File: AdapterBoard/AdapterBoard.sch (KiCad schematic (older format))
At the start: 80 parts, among them J1 Conn_01x06, J10 Conn_01x01, J11 Conn_01x02, J12 Conn_01x01, J13 Conn_01x02, J14 Conn_01x01, J15 Conn_01x02, J16 Conn_01x01, J17 Conn_01x02, J18 Conn_01x01, J19 Conn_01x02, J2 Conn_01x06, J20 Conn_01x01, J21 Conn_01x02, J22 Conn_01x01, J23 Conn_01x02, J24 Conn_01x01, J25 Conn_01x01, J26 Conn_01x06, J27 Conn_01x01, J28 Conn_01x04, J29 Conn_01x06, J3 Conn_01x06, J30 Conn_01x06, J31 Conn_01x04, J32 Conn_01x01, J33 Conn_01x06, J34 Conn_01x01, J35 Conn_01x01, J36 Conn_01x01, J37 Conn_01x01, J38 Conn_01x06, J39 Conn_01x01, J4 Conn_01x06, J40 Conn_01x04, J41 Conn_01x06, J42 Conn_01x06, J43 Conn_01x04, J44 Conn_01x01, J45 Conn_01x06, J46 Conn_01x01, J47 Conn_01x01, J48 Conn_01x06, J49 Conn_01x04, J5 Conn_01x06, J50 Conn_01x01, J51 Conn_01x06, J52 Conn_01x01, J53 Conn_01x01, J54 Conn_01x06, J55 Conn_01x04, J56 Conn_01x01, J57 Conn_01x06, J58 Conn_01x01, J59 Conn_01x04, J6 Conn_01x06, J60 Conn_02x13_Odd_Even, J61 Conn_01x04, J62 Conn_01x04, J63 Conn_01x13, J64 Conn_01x13, J7 Conn_01x06, J8 Conn_01x06, J9 Conn_01x02

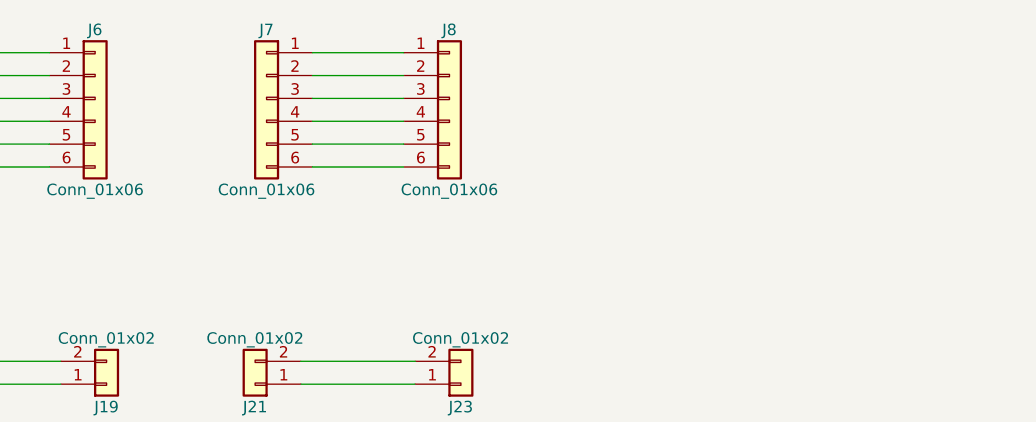
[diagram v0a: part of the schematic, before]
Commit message: Added CAD models
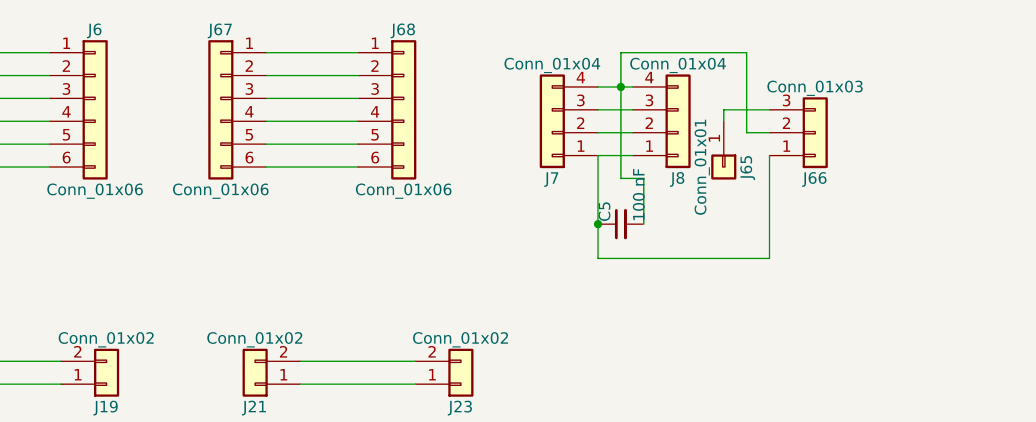
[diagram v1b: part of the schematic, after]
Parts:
- removed J7, J8: Conn_01x06, Pin_Headers:Pin_Header_Straight_1x06_Pitch2.54mm, symbol Conn_01x06
- added C5: 100 nF, Capacitors_THT:C_Disc_D5.0mm_W2.5mm_P2.50mm, symbol C_Small
- added J65: Conn_01x01, Pin_Headers:Pin_Header_Straight_1x01_Pitch2.54mm, symbol Conn_01x01
- added J66: Conn_01x03, TO_SOT_Packages_THT:TO-92_Inline_Wide, symbol Conn_01x03
- added J67, J68: Conn_01x06, Pin_Headers:Pin_Header_Straight_1x06_Pitch2.54mm, symbol Conn_01x06
- added J7, J8: Conn_01x04, Pin_Headers:Pin_Header_Straight_1x04_Pitch2.54mm, symbol Conn_01x04
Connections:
- new net: C5.1, J66.1 (Pin_1), J7.1 (Pin_1), J8.1 (Pin_1)
- new net: J7.2 (Pin_2), J8.2 (Pin_2)
- new net: J7.3 (Pin_3), J8.3 (Pin_3)
- new net: C5.2, J66.2 (Pin_2), J7.4 (Pin_4), J8.4 (Pin_4)
- new net: J65.1 (Pin_1), J66.3 (Pin_3)
- new net: J67.1 (Pin_1), J68.1 (Pin_1)
- new net: J67.2 (Pin_2), J68.2 (Pin_2)
- new net: J67.3 (Pin_3), J68.3 (Pin_3)
- new net: J67.4 (Pin_4), J68.4 (Pin_4)
- new net: J67.5 (Pin_5), J68.5 (Pin_5)
- new net: J67.6 (Pin_6), J68.6 (Pin_6)
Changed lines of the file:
@@
-$EndComp
-$Comp
-L Conn_01x06 J8
-U 1 1 614931F7
-P 6700 1400
-F 0 "J8" H 6700 1700 50  0000 C CNN
-F 1 "Conn_01x06" H 6700 1000 50  0000 C CNN
-F 2 "Pin_Headers:Pin_Header_Straight_1x06_Pitch2.54mm" H 6700 1400 50  0001 C CNN
-F 3 "" H 6700 1400 50  0001 C CNN
-	1    6700 1400
-	1    0    0    -1
-$EndComp
-$Comp
-L Conn_01x06 J7
-U 1 1 614931FD
-P 5900 1400
-F 0 "J7" H 5900 1700 50  0000 C CNN
-F 1 "Conn_01x06" H 5900 1000 50  0000 C CNN
-F 2 "Pin_Headers:Pin_Header_Straight_1x06_Pitch2.54mm" H 5900 1400 50  0001 C CNN
-F 3 "" H 5900 1400 50  0001 C CNN
-	1    5900 1400
-	-1   0    0    -1
 $EndComp
 $Comp
@@
 	4950 1700 4550 1700
 Wire Wire Line
-	6500 1200 6100 1200
-Wire Wire Line
-	6500 1300 6100 1300
-Wire Wire Line
-	6500 1400 6100 1400
-Wire Wire Line
-	6500 1500 6100 1500
-Wire Wire Line
-	6500 1600 6100 1600
-Wire Wire Line
-	6500 1700 6100 1700
-Wire Wire Line
 	1950 2700 1500 2700
 Wire Wire Line
@@
 Wire Wire Line
 	5850 6050 5850 6150
+$Comp
+L Conn_01x04 J7
+U 1 1 614A8BCB
+P 7150 1550
+F 0 "J7" H 7150 1750 50  0000 C CNN
+F 1 "Conn_01x04" H 7150 1250 50  0000 C CNN
+F 2 "Pin_Headers:Pin_Header_Straight_1x04_Pitch2.54mm" H 7150 1550 50  0001 C CNN
+F 3 "" H 7150 1550 50  0001 C CNN
+	1    7150 1550
+	-1   0    0    1
+$EndComp
+$Comp
+L Conn_01x04 J8
+U 1 1 614A8BD1
+P 7700 1550
+F 0 "J8" H 7700 1750 50  0000 C CNN
+F 1 "Conn_01x04" H 7700 1250 50  0000 C CNN
+F 2 "Pin_Headers:Pin_Header_Straight_1x04_Pitch2.54mm" H 7700 1550 50  0001 C CNN
+F 3 "" H 7700 1550 50  0001 C CNN
+	1    7700 1550
+	1    0    0    1
+$EndComp
+Wire Wire Line
+	7350 1650 7500 1650
+Wire Wire Line
+	7350 1550 7500 1550
+Wire Wire Line
+	7500 1450 7350 1450
+Wire Wire Line
+	7350 1350 7500 1350
+$Comp
+L C_Small C5
+U 1 1 614A9377
+P 7450 1950
+F 0 "C5" H 7460 2020 50  0000 L CNN
+F 1 "100 nF" H 7460 1870 50  0000 L CNN
+F 2 "Capacitors_THT:C_Disc_D5.0mm_W2.5mm_P2.50mm" H 7450 1950 50  0001 C CNN
+F 3 "" H 7450 1950 50  0001 C CNN
+	1    7450 1950
+	0    -1   -1   0
+$EndComp
+$Comp
+L Conn_01x03 J66
+U 1 1 614A96E7
+P 8300 1550
+F 0 "J66" H 8300 1750 50  0000 C CNN
+F 1 "Conn_01x03" H 8300 1350 50  0000 C CNN
+F 2 "TO_SOT_Packages_THT:TO-92_Inline_Wide" H 8300 1550 50  0001 C CNN
+F 3 "" H 8300 1550 50  0001 C CNN
+	1    8300 1550
+	1    0    0    1
+$EndComp
+Wire Wire Line
+	7350 1650 7350 2100
+Wire Wire Line
+	7550 1950 7550 1750
+Wire Wire Line
+	7550 1750 7450 1750
+Wire Wire Line
+	7450 1750 7450 1200
+Connection ~ 7450 1350
+Wire Wire Line
+	8100 1650 8100 2100
+Wire Wire Line
+	8100 2100 7350 2100
+Connection ~ 7350 1950
+$Comp
+L Conn_01x01 J65
+U 1 1 614AA427
+P 7900 1700
+F 0 "J65" H 7900 1800 50  0000 C CNN
+F 1 "Conn_01x01" H 7900 1600 50  0000 C CNN
+F 2 "Pin_Headers:Pin_Header_Straight_1x01_Pitch2.54mm" H 7900 1700 50  0001 C CNN
+F 3 "" H 7900 1700 50  0001 C CNN
+	1    7900 1700
+	0    1    1    0
+$EndComp
+Wire Wire Line
+	8000 1550 8100 1550
+Wire Wire Line
+	8000 1550 8000 1200
+Wire Wire Line
+	8000 1200 7450 1200
+Wire Wire Line
+	7900 1500 7900 1450
+Wire Wire Line
+	7900 1450 8100 1450
+$Comp
+L Conn_01x06 J68
+U 1 1 614BD3BF
+P 6500 1400
+F 0 "J68" H 6500 1700 50  0000 C CNN
+F 1 "Conn_01x06" H 6500 1000 50  0000 C CNN
+F 2 "Pin_Headers:Pin_Header_Straight_1x06_Pitch2.54mm" H 6500 1400 50  0001 C CNN
+F 3 "" H 6500 1400 50  0001 C CNN
+	1    6500 1400
+	1    0    0    -1
+$EndComp
+$Comp
+L Conn_01x06 J67
+U 1 1 614BD3C5
+P 5700 1400
+F 0 "J67" H 5700 1700 50  0000 C CNN
+F 1 "Conn_01x06" H 5700 1000 50  0000 C CNN
+F 2 "Pin_Headers:Pin_Header_Straight_1x06_Pitch2.54mm" H 5700 1400 50  0001 C CNN
+F 3 "" H 5700 1400 50  0001 C CNN
+	1    5700 1400
+	-1   0    0    -1
+$EndComp
+Wire Wire Line
+	6300 1200 5900 1200
+Wire Wire Line
+	6300 1300 5900 1300
+Wire Wire Line
+	6300 1400 5900 1400
+Wire Wire Line
+	6300 1500 5900 1500
+Wire Wire Line
+	6300 1600 5900 1600
+Wire Wire Line
+	6300 1700 5900 1700
 $EndSCHEMATC

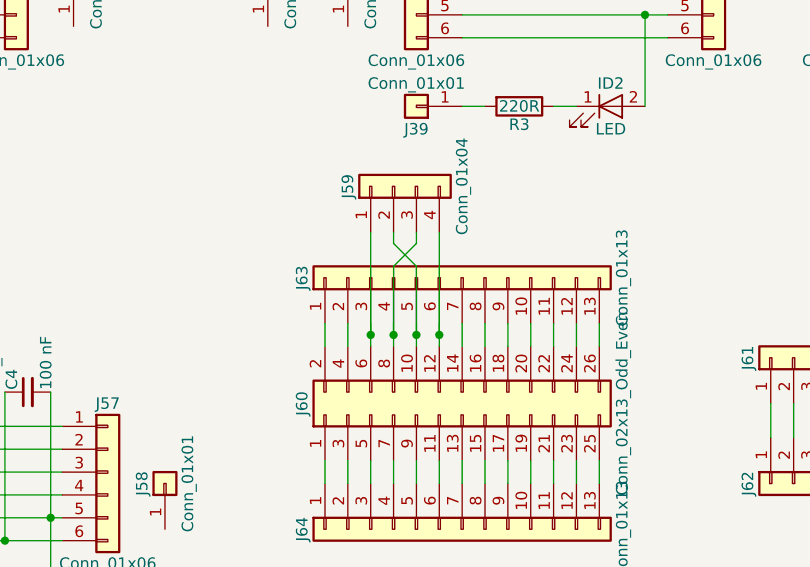
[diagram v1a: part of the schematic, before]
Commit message: Added second microphone to keypad
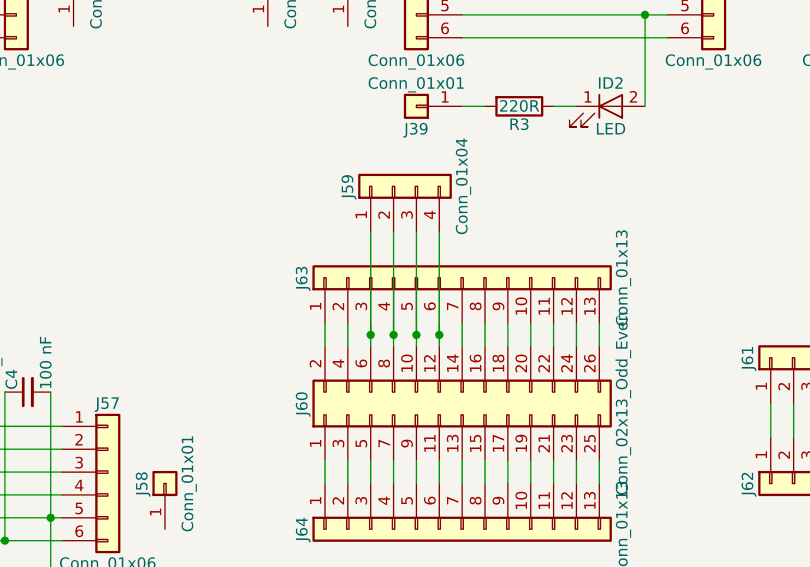
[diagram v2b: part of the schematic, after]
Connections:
- net at J60.10 (Pin_10), J63.5 (Pin_5): now also J59.3 (Pin_3); no longer J59.2 (Pin_2)
- net at J60.8 (Pin_8), J63.4 (Pin_4): now also J59.2 (Pin_2); no longer J59.3 (Pin_3)
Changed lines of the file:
@@
 $EndComp
 Wire Wire Line
-	6250 5200 6150 5100
-Wire Wire Line
-	6150 5100 6150 5050
+	6150 5050 6150 5500
 Wire Wire Line
 	6050 5450 6050 5550
@@
 	6250 5450 6250 5550
 Wire Wire Line
-	6250 5500 6250 5200
+	6250 5050 6250 5500
 Connection ~ 6250 5500
 Wire Wire Line
 	6150 5450 6150 5550
-Wire Wire Line
-	6150 5500 6150 5200
-Wire Wire Line
-	6150 5200 6250 5100
-Wire Wire Line
-	6250 5100 6250 5050
 Connection ~ 6150 5500
 Wire Wire Line
